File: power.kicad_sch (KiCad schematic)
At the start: 111 parts, among them J1 Molex_Nano-Fit_1x2_SMD_105430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, J2 USB-C_GCT_USB4105-GF-A, Q1 2N7002_SOT-23-3, Q4 2N7002_SOT-23-3, U1 TPS566231P, U2 TPS566231P, U3 TPS566231P, U4 TPS566231P, U5 TPS566231P

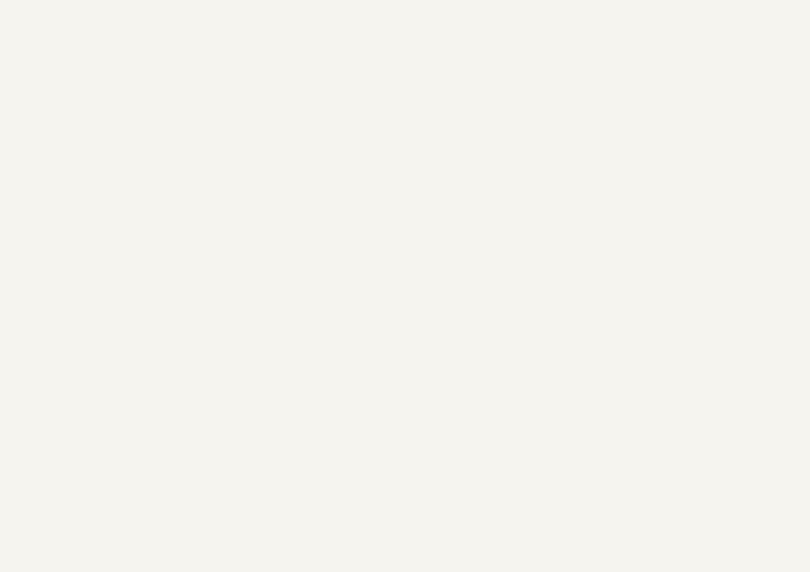
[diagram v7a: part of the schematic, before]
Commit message: [#88407] Sch: Add PCIe ref clock; Add ICT testpoints; Add fan TVS
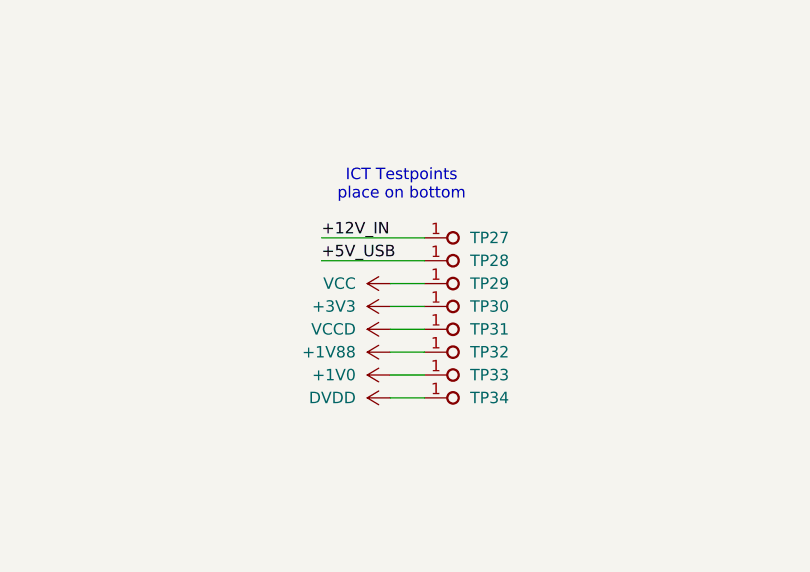
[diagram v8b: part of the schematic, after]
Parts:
- added TP27, TP28, TP29, TP30, TP31, TP32, TP33, TP34: TP_1mm_SMD, antmicro-footprints:TP_SMD_1mm, symbol antmicroTestPoints:TP_1mm_SMD
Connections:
- net +12V_IN: now also TP27.1
- net +1V0: now also TP33.1
- net +1V88: now also TP32.1
- net +3V3: now also TP30.1
- net +5V_USB: now also TP28.1
- net DVDD: now also TP34.1
- net VCC: now also TP29.1
- net VCCD: now also TP31.1
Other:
- note added: "ICT Testpoints place on bottom"
